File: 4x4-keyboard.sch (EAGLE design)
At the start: 76 parts, among them J1 M01X1-100MIL-PTH, J10 M01X1-100MIL-PTH, J11 M01X1-100MIL-PTH, J12 M01X1-100MIL-PTH, J13 M01X1-100MIL-PTH, J14 M01X1-100MIL-PTH, J15 M01X1-100MIL-PTH, J16 M01X1-100MIL-PTH, J17 M01X1-100MIL-PTH, J18 M01X1-100MIL-PTH, J19 M01X1-100MIL-PTH, J2 M01X1-100MIL-PTH, J20 M01X1-100MIL-PTH, J21 M01X1-100MIL-PTH, J22 M01X1-100MIL-PTH, J23 M01X1-100MIL-PTH, J24 M01X1-100MIL-PTH, J25 M12-100MIL, J26 M12-100MIL, J3 M01X1-100MIL-PTH, J4 M01X1-100MIL-PTH, J5 M01X1-100MIL-PTH, J6 M01X1-100MIL-PTH, J7 M01X1-100MIL-PTH, J8 M01X1-100MIL-PTH, J9 M01X1-100MIL-PTH

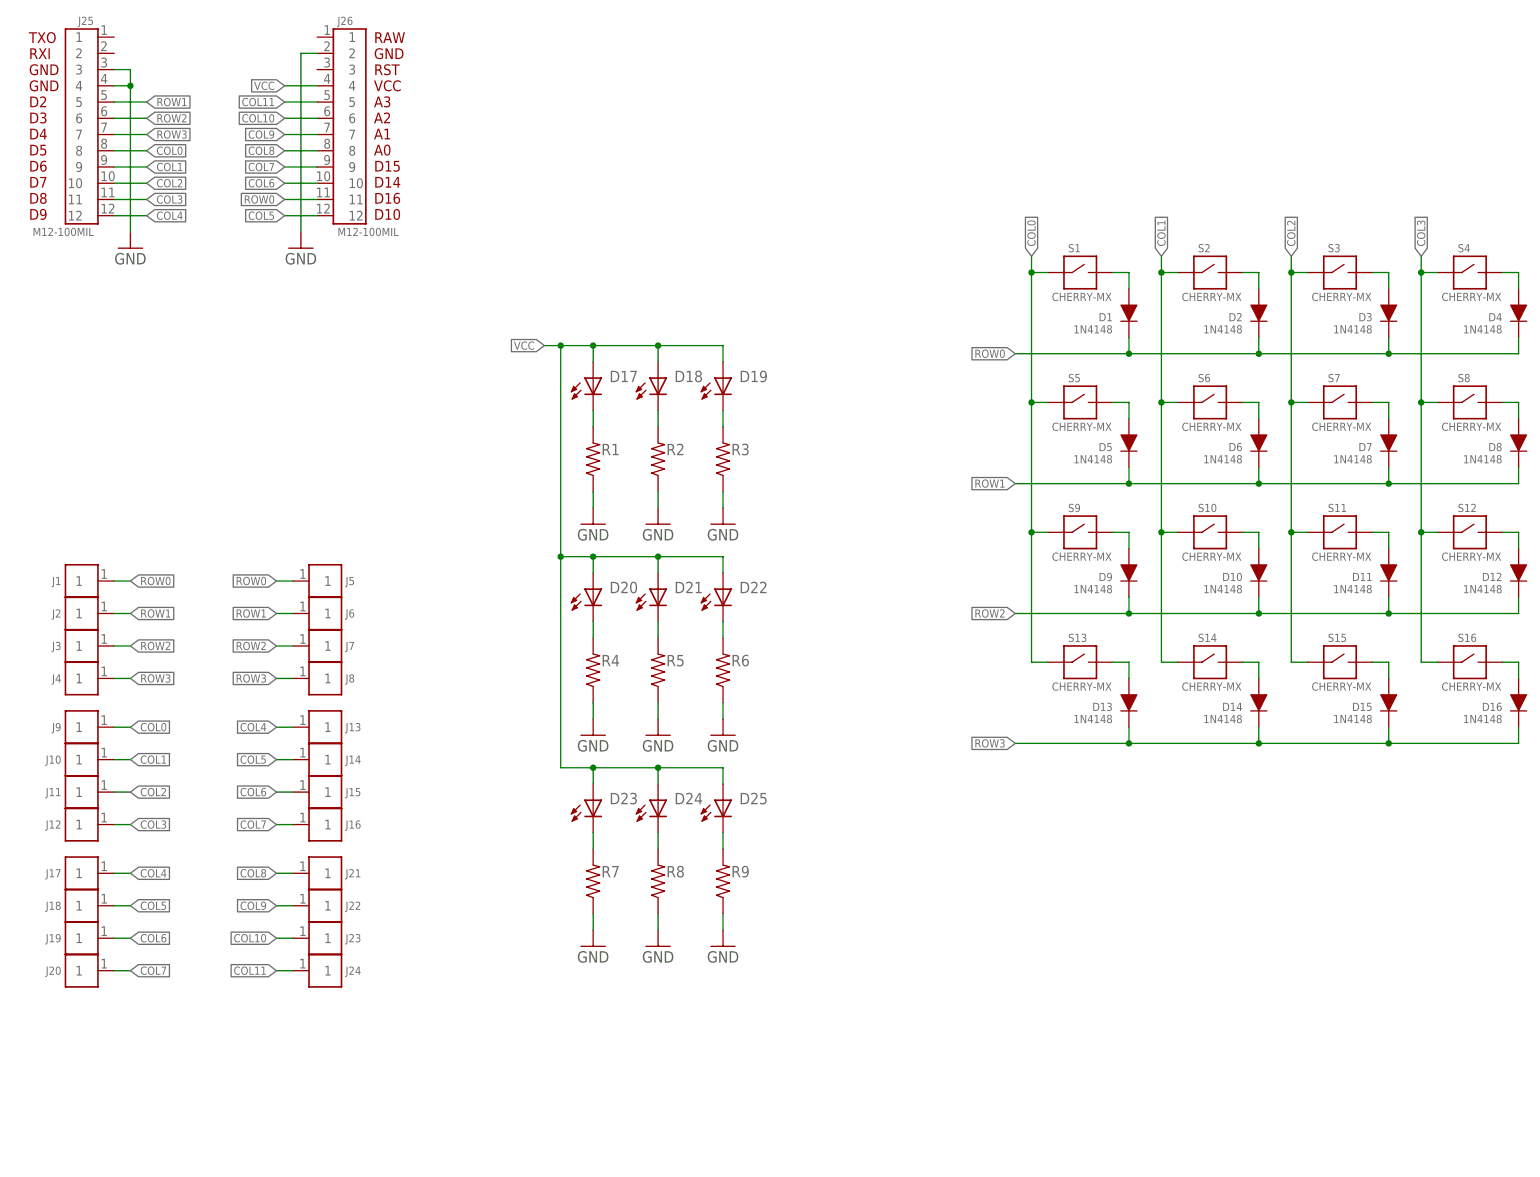
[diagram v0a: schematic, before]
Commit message: Update layout
- Remove extensible connectors
- Add backlight 3mm leds instead of frontlight smd
- Add I/O-controlled mosfet for driving dimmable backlight
- Add reset switch
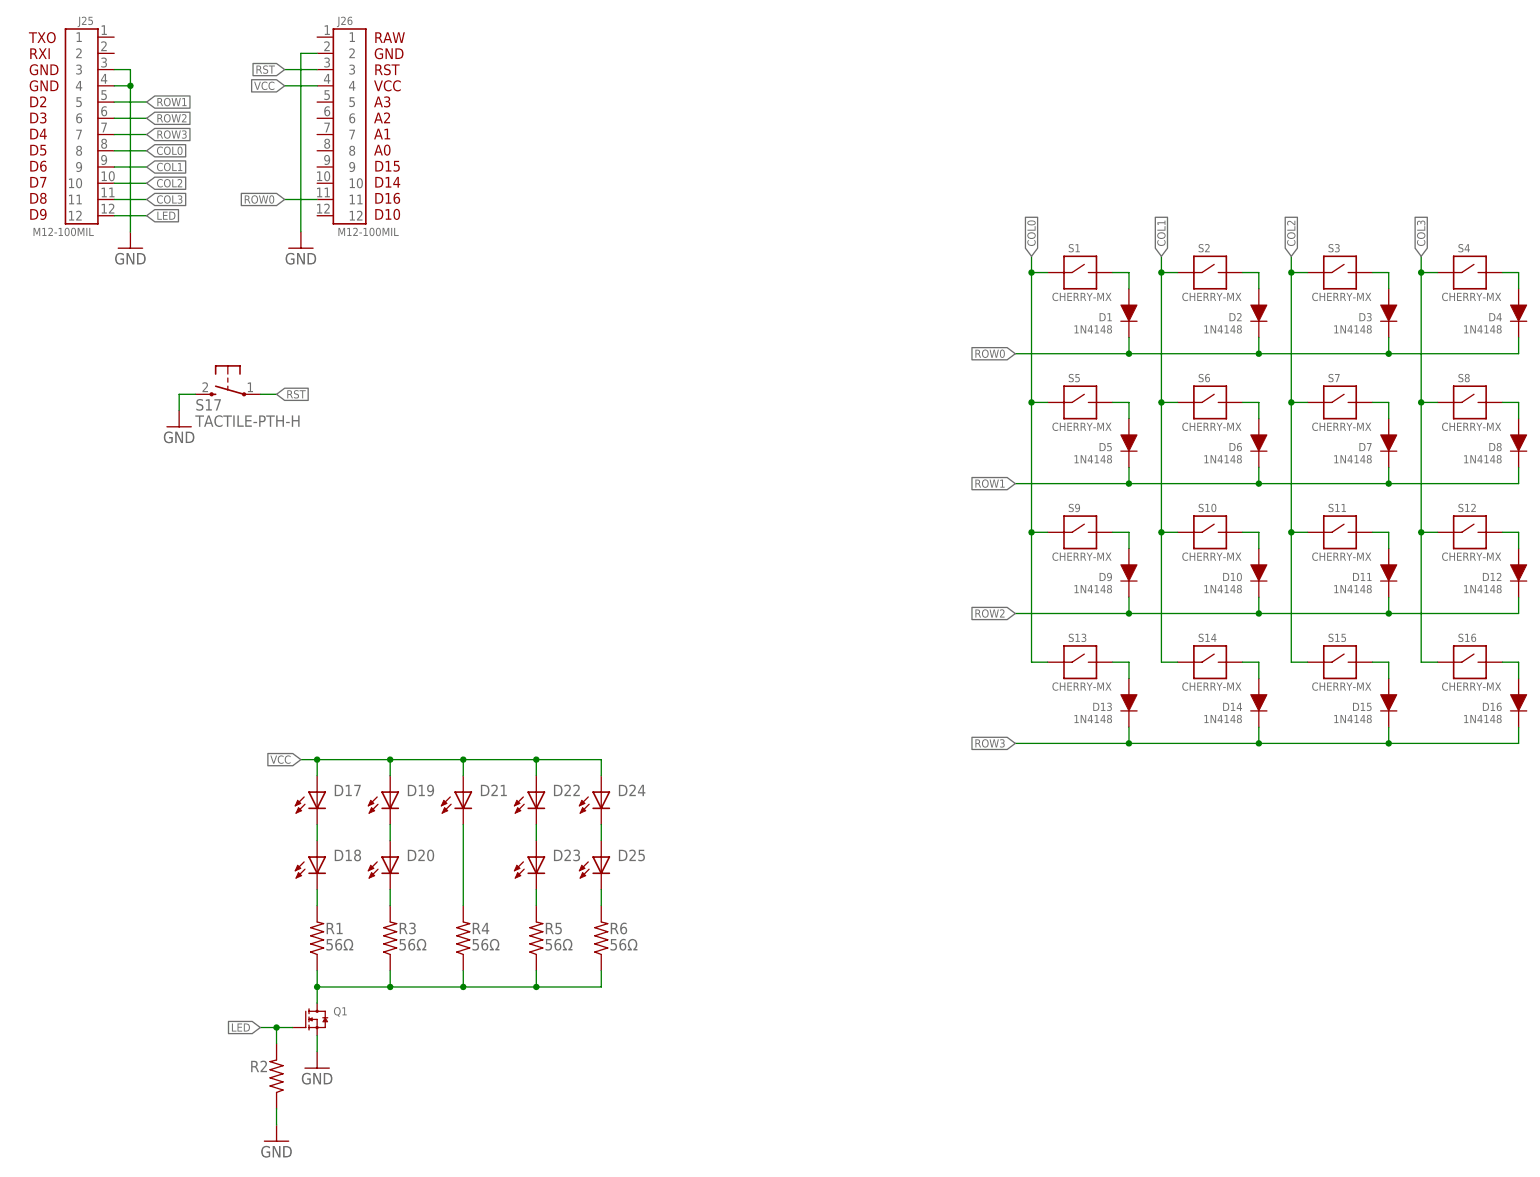
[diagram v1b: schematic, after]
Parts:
- removed J1, J10, J11, J12, J13, J14, J15, J16, J17, J18, J19, J2, J20, J21, J22, J23, J24, J3, J4, J5, J6, J7, J8, J9: M01X1-100MIL-PTH, Connectors:M01X1-100MIL-PTH
- removed R7, R8, R9: (no value), Passives:RESISTOR-0603
- added Q1: (no value), Passives:N-MOSFET-TO-92
- added S17: TACTILE-PTH-H, Passives:TACTILE-PTH-H
- D17, D18, D19, D20, D21, D22, D23, D24, D25: device Passives:LED-0603 -> Passives:LED-3MM
- R1, R3, R4, R5, R6: value (none) -> 56Ω; device Passives:RESISTOR-0603 -> Passives:RESISTOR-PTH
- R2: device Passives:RESISTOR-0603 -> Passives:RESISTOR-PTH
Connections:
- removed net COL10: J23.1, J26.6
- removed net COL11: J24.1, J26.5
- removed net COL4: J13.1, J17.1, J25.12
- removed net COL5: J14.1, J18.1, J26.12
- removed net COL6: J15.1, J19.1, J26.10
- removed net COL7: J16.1, J20.1, J26.9
- removed net COL8: J21.1, J26.8
- removed net COL9: J22.1, J26.7
- removed net N$26: D22.C, R6.2
- removed net N$27: D23.C, R7.2
- removed net N$29: D25.C, R9.2
- new net LED: J25.12, Q1.GATE, R2.2
- new net N$34: D19.C, D20.A
- new net N$35: D20.C, R3.2
- new net N$36: D18.C, R1.2
- new net N$37: D17.C, D18.A
- new net RST: J26.3, S17.1
- net COL0: no longer J9.1
- net COL1: no longer J10.1
- net COL2: no longer J11.1
- net COL3: no longer J12.1
- net GND: now also Q1.SOURCE, S17.3; no longer R1.1, R3.1, R4.1, R5.1, R6.1, R7.1, R8.1, R9.1
- net N$22: now also D21.C, R4.2; no longer D18.C, R2.2
- net N$23: now also D24.C, D25.A; no longer D19.C, R3.2
- net N$24: now also D22.C, D23.A; no longer D20.C, R4.2
- net N$25: now also D23.C; no longer D21.C
- net N$28: now also D25.C, R6.2; no longer D24.C, R8.2
- net N$6: now also Q1.DRAIN, R1.1, R3.1, R4.1, R5.1, R6.1; no longer D17.C, R1.2
- net ROW0: no longer J1.1, J5.1
- net ROW1: no longer J2.1, J6.1
- net ROW2: no longer J3.1, J7.1
- net ROW3: no longer J4.1, J8.1
- net VCC: no longer D18.A, D20.A, D23.A, D25.A
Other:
- moved on the sheet: D17, D18, D19, D20, D21, D22, D23, D24, D25, R1, R2, R3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
